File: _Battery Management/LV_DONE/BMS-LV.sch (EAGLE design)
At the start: 114 parts, among them J1 M1x5, J2 M1x4, J3 M1x4, J4 M1x4, J5 M1x2, J6 MX150L, J8 M1x5, J9 M80022232081-2, K1 ADJ14024, Q2 40V 0.2A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

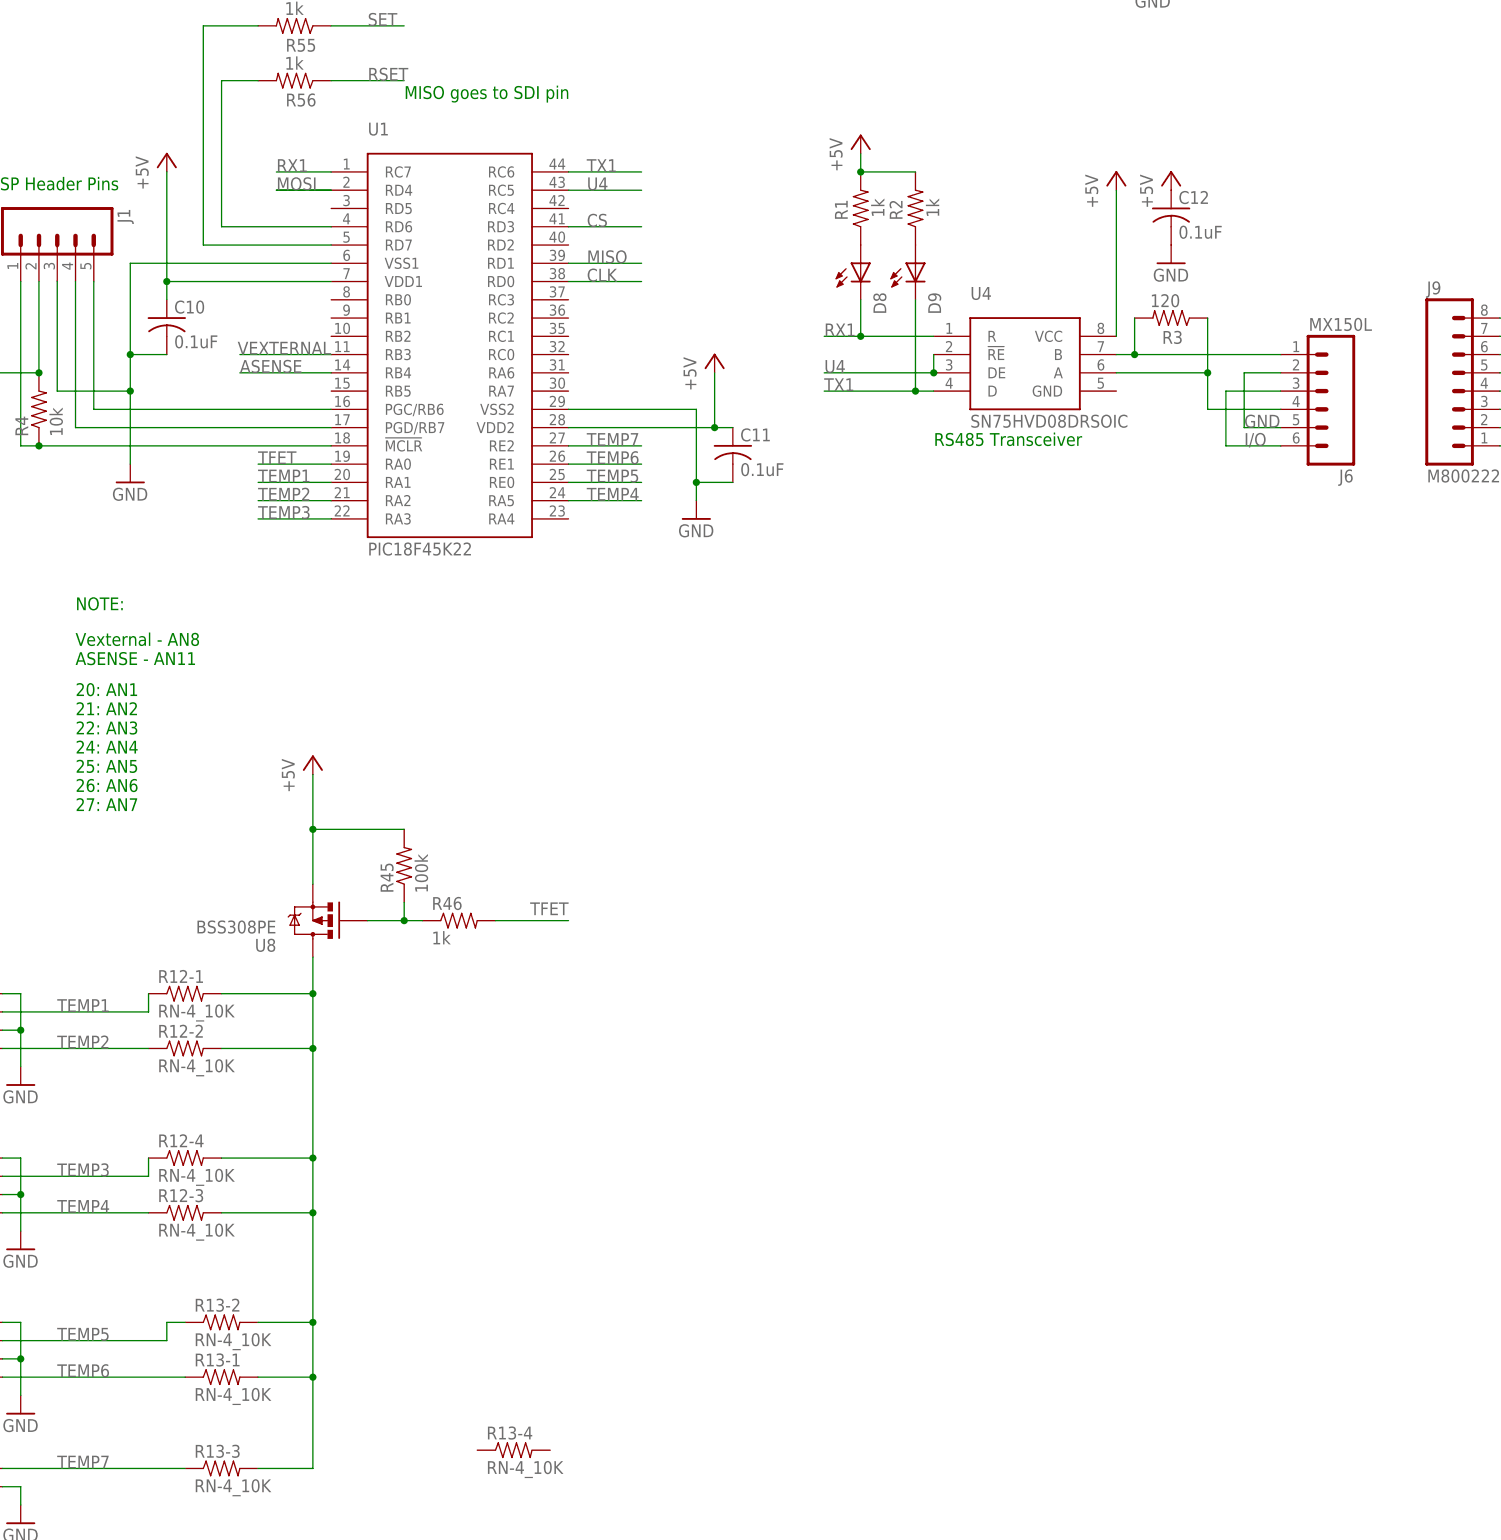
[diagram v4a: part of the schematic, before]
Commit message: 
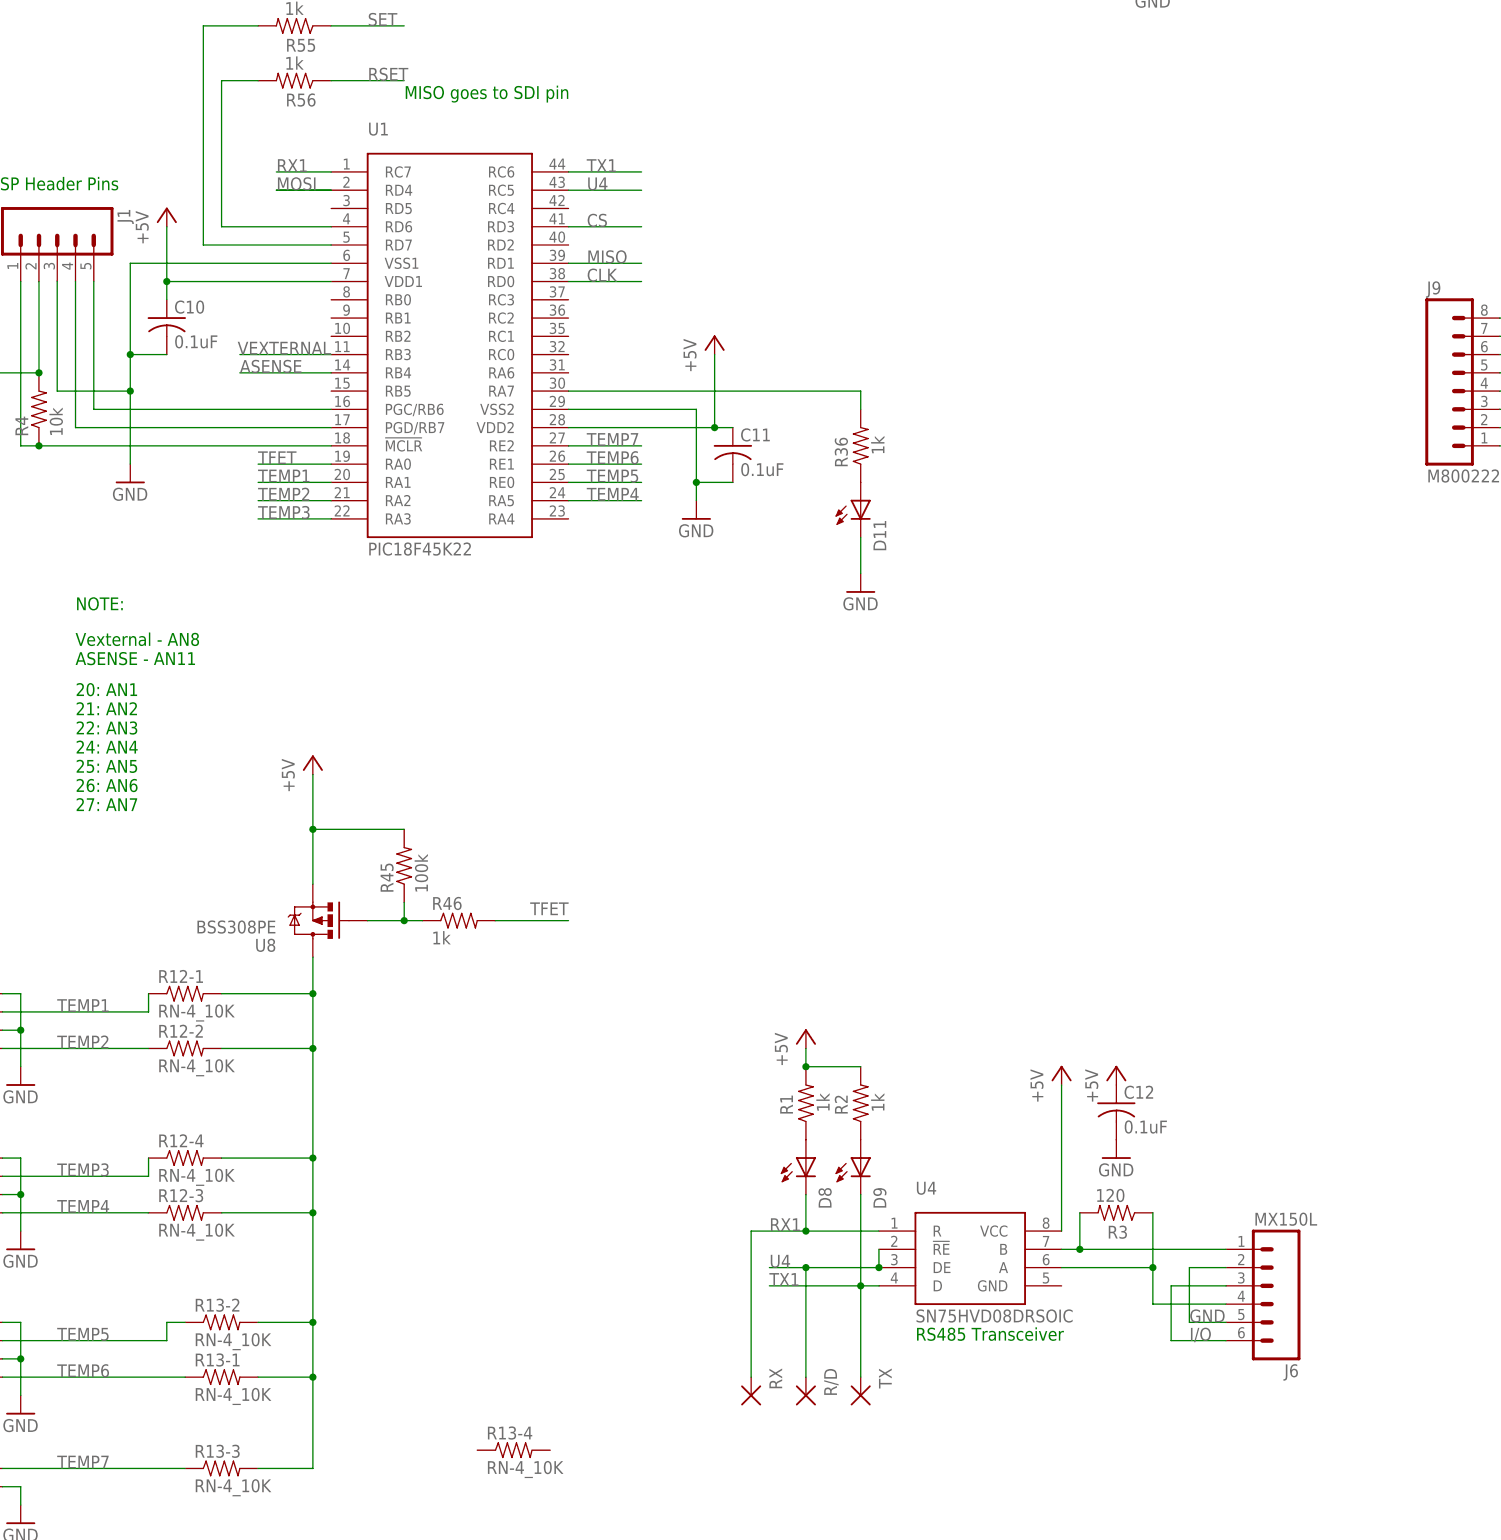
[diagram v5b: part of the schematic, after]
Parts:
- added D11: LED_AMBER, FSAE Electric:LED_AMBER
- added R/D, RX, TX: TPSMD, FSAE Electric:TPSMD
- added R36: 1k, FSAE Electric:RES_1K_5%
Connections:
- removed net VDD1: C10.+, U1.VDD1
- new net N$14: R36.2, U1.RA7
- new net N$5: D11.A, R36.1
- net +5V: now also C10.+, U1.VDD1
- net GND: now also D11.C
- net RX1: now also RX.P$1
- net TX1: now also TX.P$1
- net U4: now also R/D.P$1
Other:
- moved on the sheet: C12, D8, D9, J6, R1, R2, R3, U4
